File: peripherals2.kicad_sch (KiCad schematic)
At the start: 34 parts, among them J7 MSD-4-A, J8 DISPLAY CONN, Q2 SL2301S, Q3 T2N7002AK,LM, U8 GSDA213

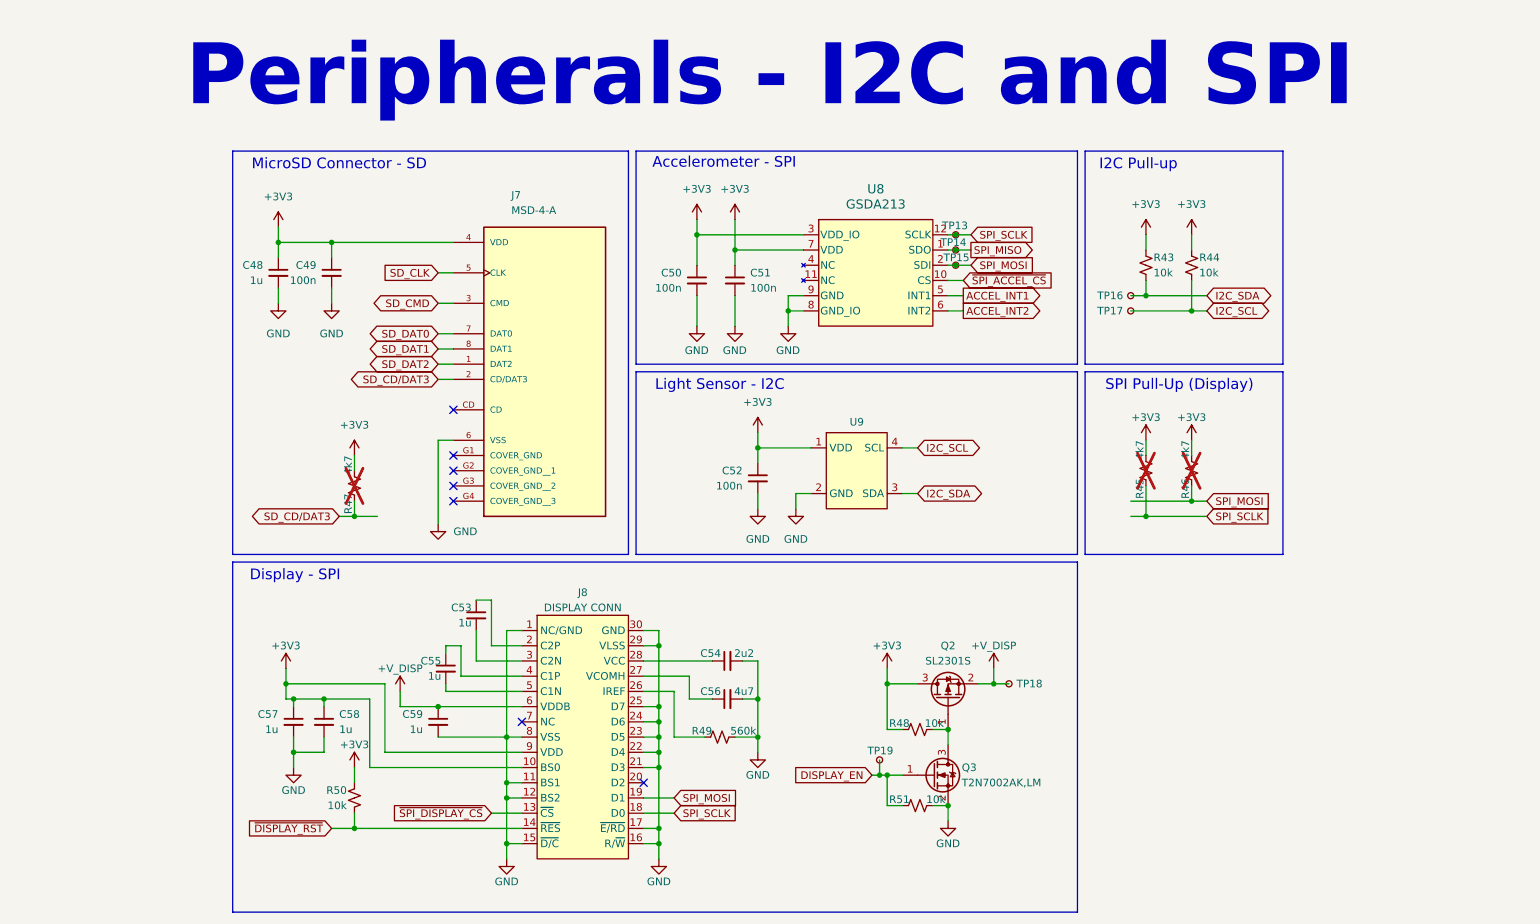
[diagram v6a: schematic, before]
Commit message: feat:  adds requested components
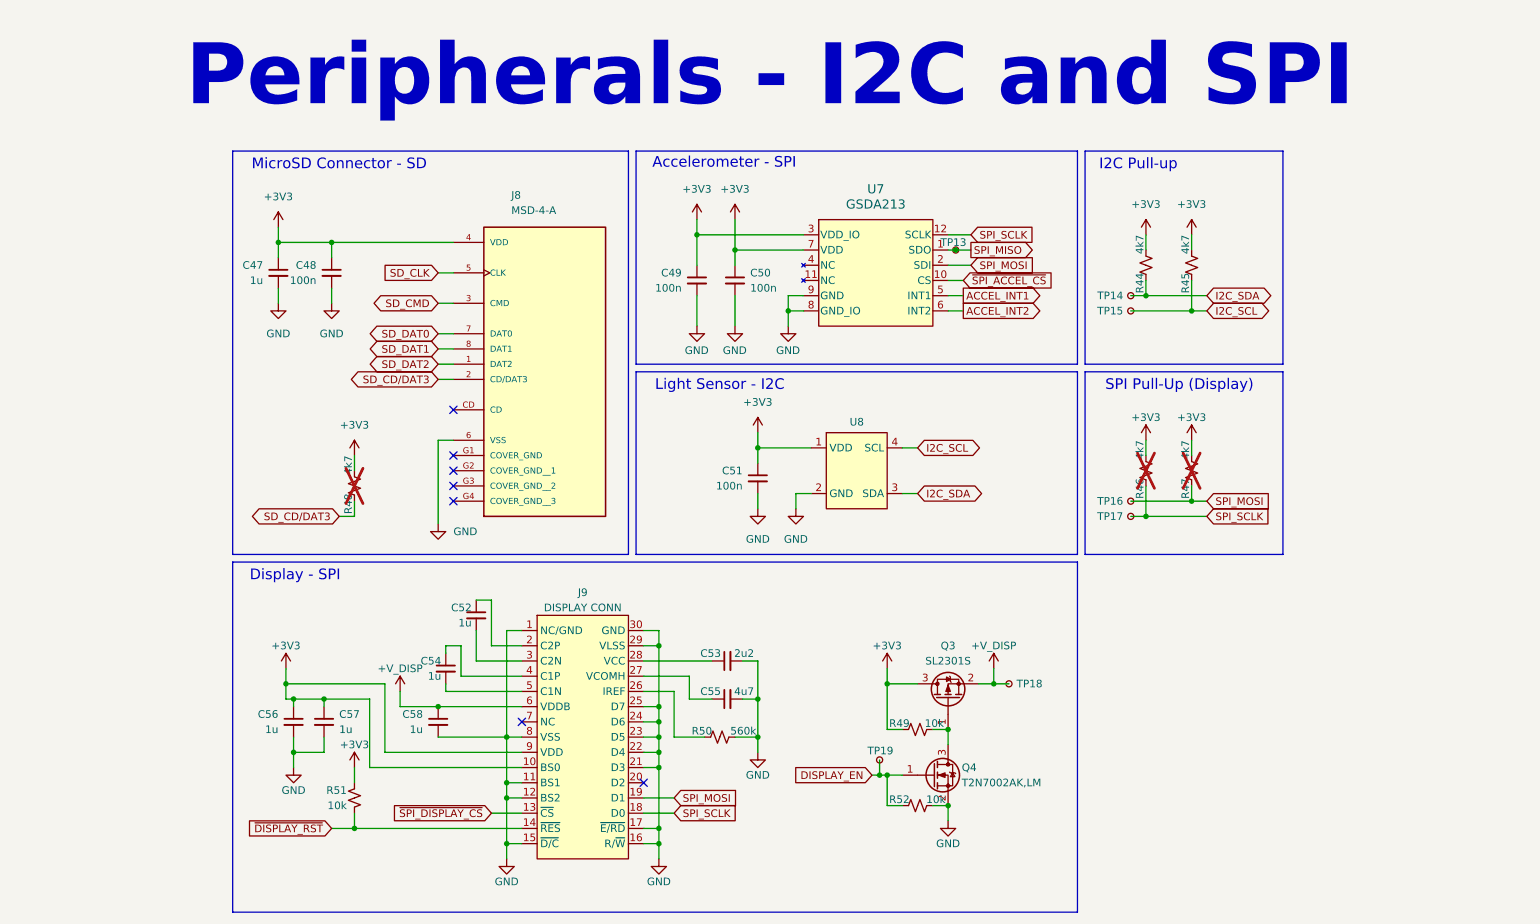
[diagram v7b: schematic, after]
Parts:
- removed R43: 10k, Resistor_SMD:R_0402_1005Metric, symbol Device:R_Small_US
- added R45: 4k7, Resistor_SMD:R_0402_1005Metric, symbol Device:R_Small_US
- R44: value 10k -> 4k7; MPN RC0402JR-0710KL -> RC0402JR-074K7L
- renumbered C48 to C47, C49 to C48, C50 to C49, C51 to C50, C52 to C51, C53 to C52, C54 to C53, C55 to C54, C56 to C55, C57 to C56, C58 to C57, C59 to C58, J7 to J8, J8 to J9, Q2 to Q3, Q3 to Q4, R45 to R46, R46 to R47, R47 to R48, R48 to R49, R49 to R50, R50 to R51, R51 to R52, TP14 to TP13, TP16 to TP14, TP17 to TP15, TP15 to TP16, TP13 to TP17, U8 to U7, U9 to U8
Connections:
- net +3V3: now also R44.2, R45.2; no longer R44.1
- net I2C_SCL: now also R45.1; no longer R44.2
- net I2C_SDA: now also R44.1
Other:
- moved on the sheet: TP16, TP17

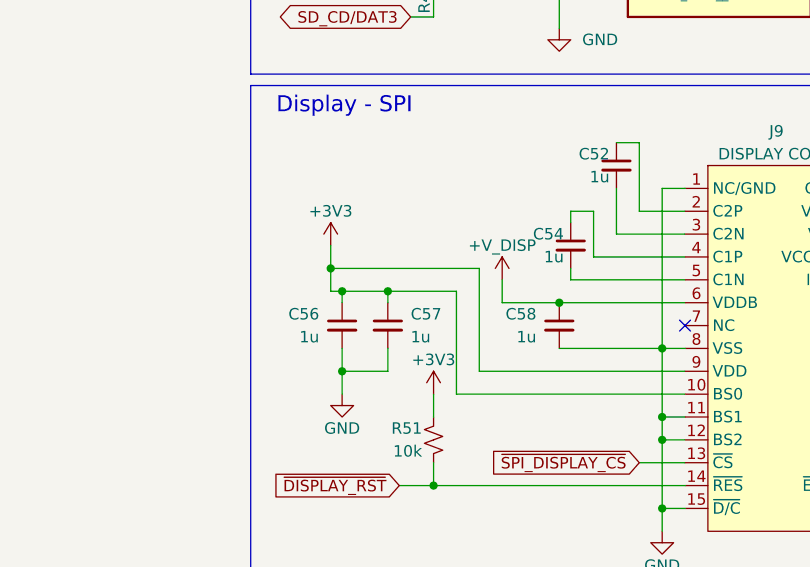
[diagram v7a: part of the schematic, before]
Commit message: refac: changes peripherals2 placement a bit
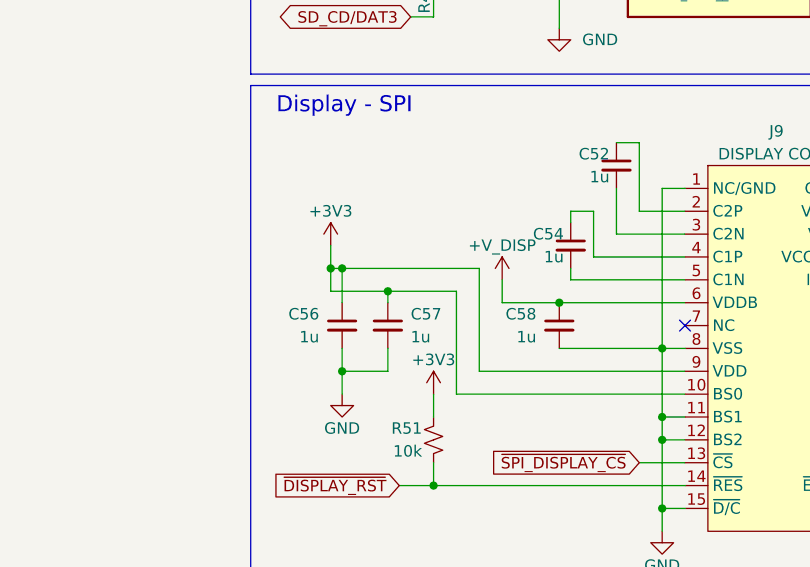
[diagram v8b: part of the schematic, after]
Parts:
- C53: footprint Capacitor_SMD:C_0603_1608Metric -> Capacitor_SMD:C_0402_1005Metric; MPN CL10B225KP8NNNC -> CL05A225KO5NQNC
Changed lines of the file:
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@@
+	)
+	(junction
+		(at 72.39 125.73)
+		(diameter 0)
+		(color 0 0 0 0)
 	)
 	(junction
@@
 	)
 	(junction
-		(at 72.39 128.27)
-		(diameter 0)
-		(color 0 0 0 0)
-	)
-	(junction
 		(at 133.35 119.38)
 		(diameter 0)
@@
 	(wire
 		(pts
+			(xy 72.39 125.73) (xy 87.63 125.73)
+		)
+		(stroke
+			(width 0)
+			(type default)
+		)
+	)
+	(wire
+		(pts
 			(xy 181.61 53.34) (xy 182.88 53.34)
 		)
@@
 	(wire
 		(pts
+			(xy 72.39 125.73) (xy 72.39 129.54)
+		)
+		(stroke
+			(width 0)
+			(type default)
+		)
+	)
+	(wire
+		(pts
 			(xy 130.81 147.32) (xy 135.89 147.32)
 		)
@@
 	(wire
 		(pts
-			(xy 72.39 128.27) (xy 77.47 128.27)
-		)
-		(stroke
-			(width 0)
-			(type default)
-		)
-	)
-	(wire
-		(pts
 			(xy 105.41 111.76) (xy 102.87 111.76)
 		)
@@
 	(wire
 		(pts
-			(xy 71.12 128.27) (xy 72.39 128.27)
+			(xy 71.12 128.27) (xy 77.47 128.27)
 		)
 		(stroke
@@
 	(wire
 		(pts
-			(xy 72.39 128.27) (xy 72.39 129.54)
-		)
-		(stroke
-			(width 0)
-			(type default)
-		)
-	)
-	(wire
-		(pts
 			(xy 158.75 86.36) (xy 149.86 86.36)
 		)
@@
 	(wire
 		(pts
-			(xy 71.12 125.73) (xy 87.63 125.73)
+			(xy 71.12 125.73) (xy 72.39 125.73)
 		)
 		(stroke
@@
 			)
 		)
-		(property "Footprint" "Capacitor_SMD:C_0603_1608Metric"
+		(property "Footprint" "Capacitor_SMD:C_0402_1005Metric"
 			(at 144.78 121.92 0)
 			(effects
@@
 			)
 		)
-		(property "Datasheet" "https://www.digikey.com.br/en/products/detail/samsung-electro-mechanics/CL10B225KP8NNNC/3886792"
+		(property "Datasheet" "https://www.digikey.com.br/pt/products/detail/samsung-electro-mechanics/CL05A225KO5NQNC/3887119"
 			(at 144.78 121.92 0)
 			(effects
@@
 			)
 		)
-		(property "MPN" "CL10B225KP8NNNC"
+		(property "MPN" "CL05A225KO5NQNC"
 			(at 144.78 121.92 0)
 			(effects
